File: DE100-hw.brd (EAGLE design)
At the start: 96.5 x 71.8 mm, 50 parts, among them IC3 74HC14D, IC4 74HC14D, U1 TLP521-4(GB), U2 TLP521-4(GB), X4 JST-XH-10-PIN-LONG-PAD, X5 JST-XH-04-PIN-LONG-PAD, X6 JST-XH-03-PIN-LONG-PAD

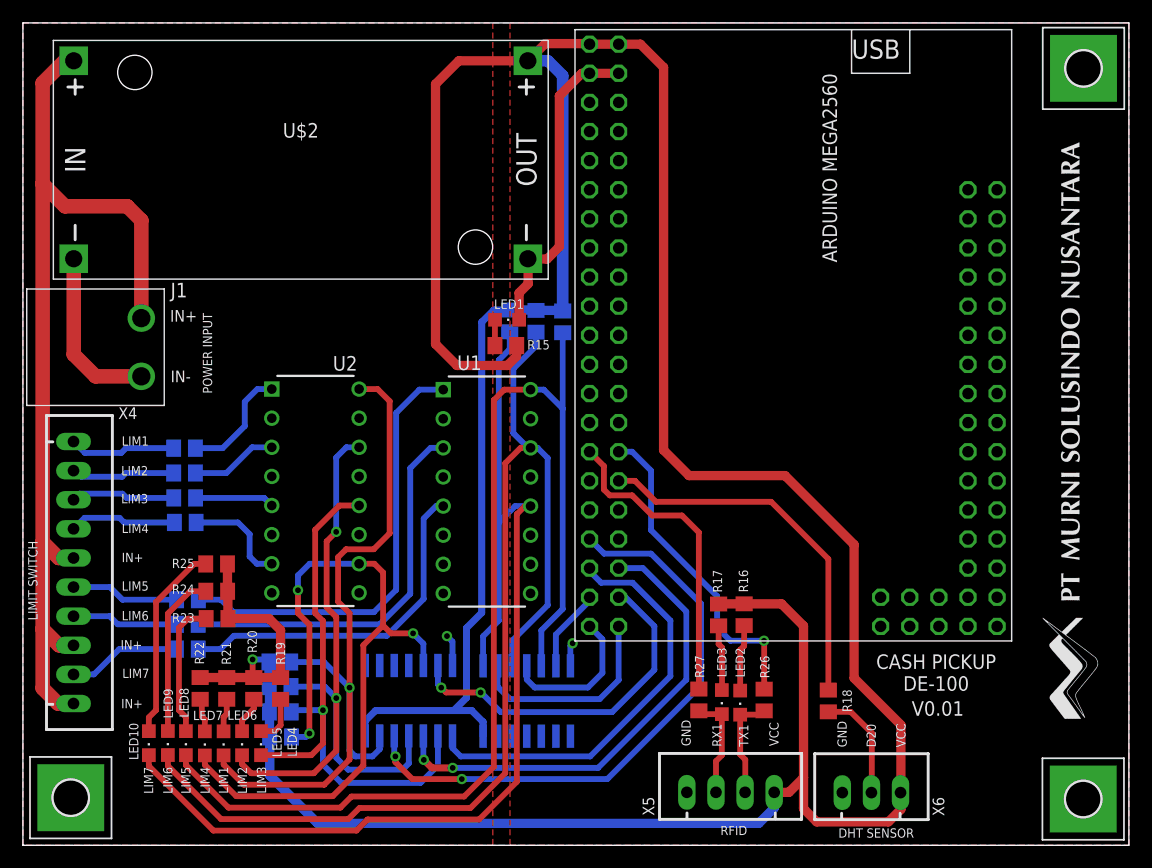
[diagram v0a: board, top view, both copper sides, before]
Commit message: add power protection
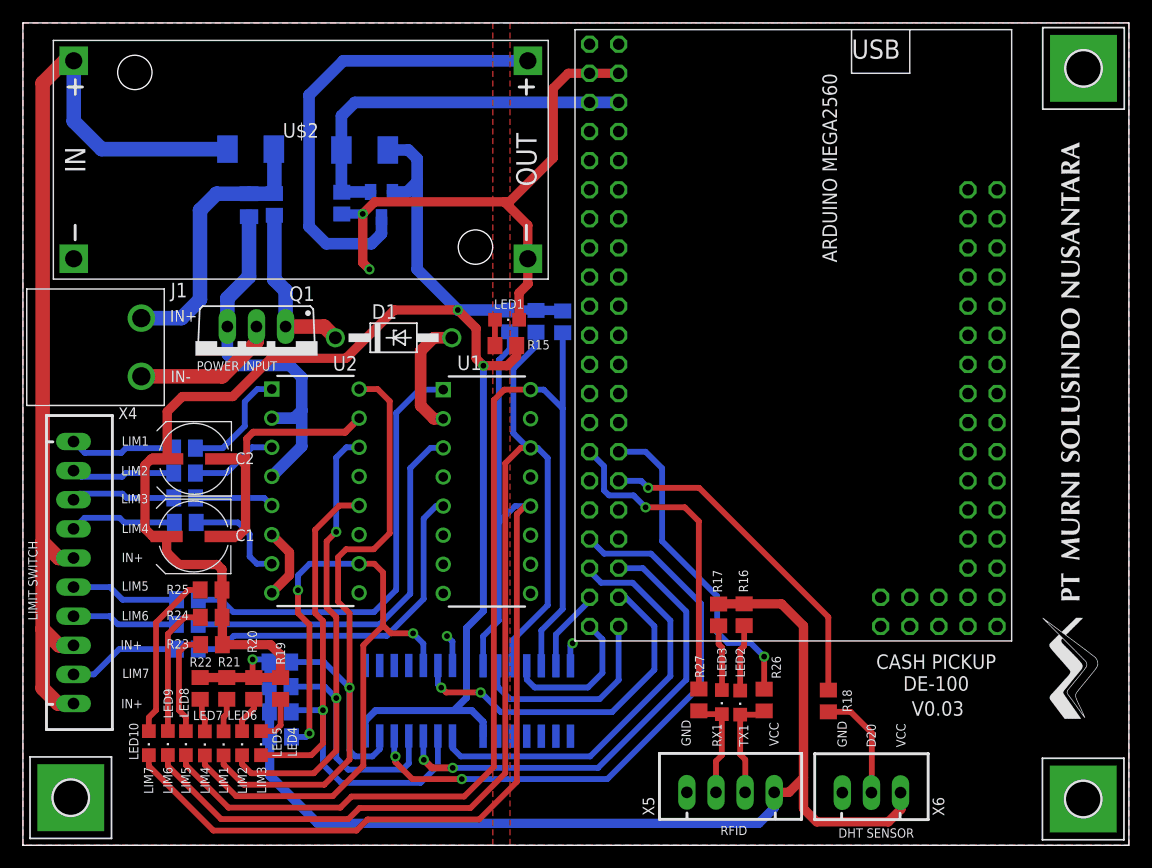
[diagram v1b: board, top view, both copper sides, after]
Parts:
- added C1, C2: 47u, rcl:UD-6,3X5,8_NICHICON
- added C3: 100n, rcl:C0805K
- added D1: 1N4728, diode:DO41Z10
- added D4, D5: (no value), diode:DO-214AC
- added Q1: IRF540, transistor-power:TO220BV
- added R28: 100k, rcl:R0805
- added R29: 10k, rcl:R0805
- added U$5: AO3401, AO3401:SOT23
- moved R23 2.32 mm to (49.5, 28.2)
- moved R24 2.32 mm to (49.4, 30.6)
- moved R25 2.32 mm to (49.4, 33.0)
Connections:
- new net N$1: J1.2, Q1.D
- new net N$2: U$2.OUT+, U$5.3
- new net N$3: D1.C, Q1.G, R28.1
- new net N$4: C3.1, D4.A, J1.1, R28.2
- new net V_USB: D5.A, R29.2, U$1.+5V.1, U$1.+5V.2, U$5.1
- net +5V: now also C1.+, C2.+, D5.C, U$5.2; no longer U$1.VIN.1, U$1.VIN.2, U$2.OUT+
- net GND: now also C1.-, C2.-, R29.1
- net GND-ISO: now also C3.2, D1.A, Q1.S; no longer J1.2
- net VCC-ISO: now also D4.C; no longer J1.1
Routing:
- net +5V: track 330.9 -> 253.8 mm, vias 1 -> 3
- net GND: track 32.8 -> 77.5 mm, vias 2 -> 4
- net N$2: track 0.00 -> 40.6 mm
- net GND-ISO: track 15.0 -> 49.5 mm
- net V_USB: track 0.00 -> 33.9 mm
- net N$4: track 0.00 -> 24.6 mm
- net N$3: track 0.00 -> 14.9 mm
- net N$1: track 0.00 -> 12.6 mm
- net DHT: track 32.6 -> 29.6 mm, vias 0 -> 1
- net N$50: track 12.0 -> 9.31 mm
- net N$52: track 17.2 -> 14.8 mm
- net N$51: track 14.4 -> 11.9 mm
- net VCC-ISO: track 84.6 -> 85.8 mm
- net RX-RFID: track 27.3 -> 27.9 mm, vias 0 -> 1
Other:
- board text added: "V0.03"
- board text removed: "V0.01"
